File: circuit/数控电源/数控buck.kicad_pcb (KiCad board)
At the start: 2 copper layers, 60 x 60 mm, 79 parts, among them J1 Conn_01x06_MountingPin, J2 Conn_01x02, J3 Conn_01x02, J4 Conn_01x04_MountingPin, Q1 BSC070N10NS3G, Q2 BSC070N10NS3G, SW1 SW_Push, U1 STM32F334R8Tx, U2 LM5164DDA, U3 LM1117DT-3.3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

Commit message: finish circuir_V1.0
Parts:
- removed C18, C20, C21: 10p, Capacitor_SMD:C_0603_1608Metric
- removed C19: 1n, Capacitor_SMD:C_0603_1608Metric
- removed J3: Conn_01x02, Connector_AMASS:AMASS_XT30PW-M_1x02_P2.50mm_Horizontal
- added C36: 10u, Capacitor_SMD:C_1206_3216Metric, F.Cu at (131.5, 26.0)
- added C37: 22u, Capacitor_SMD:C_0805_2012Metric_Pad1.18x1.45mm_HandSolder, F.Cu at (125.5, 54.5)
- added C38: 10u, Capacitor_SMD:C_1206_3216Metric, F.Cu at (131.5, 29.2)
- added J5: Conn_01x02, Connector_AMASS:AMASS_XT30U-F_1x02_P5.0mm_Vertical, F.Cu at (162.2, 60.8)
- C1, C11, C2, C3, C4, C5, D1, L1, R1, R2, R3, R4, SW1, U2, U4: moved to F.Cu
- C12, C13: footprint Capacitor_SMD:CP_Elec_16x17.5 -> Capacitor_SMD:CP_Elec_10x10.5
- C17: value 10p -> 100n; moved to B.Cu
- C22, C23, R20: moved to B.Cu
- C31: footprint Capacitor_SMD:CP_Elec_6.3x7.7 -> Capacitor_Tantalum_SMD:CP_EIA-7343-31_Kemet-D
- C6: value C_Polarized -> 22u; footprint Capacitor_SMD:CP_Elec_6.3x4.5 -> Capacitor_SMD:C_0805_2012Metric_Pad1.18x1.45mm_HandSolder; moved to F.Cu
- J2: footprint Connector_AMASS:AMASS_XT30PW-F_1x02_P2.50mm_Horizontal -> Connector_AMASS:AMASS_XT30U-M_1x02_P5.0mm_Vertical; moved to F.Cu
- R12, R13: value 82 -> 1; moved to B.Cu
- R14: value 1.2k -> 1; moved to B.Cu
- R15: value 1.2k -> R; footprint Resistor_SMD:R_0603_1608Metric_Pad0.98x0.95mm_HandSolder -> Resistor_SMD:R_0805_2012Metric_Pad1.20x1.40mm_HandSolder
- R19: value 2 -> R; footprint Resistor_SMD:R_0603_1608Metric_Pad0.98x0.95mm_HandSolder -> Resistor_SMD:R_0805_2012Metric_Pad1.20x1.40mm_HandSolder; moved to B.Cu
- R9: footprint Resistor_SMD:R_0603_1608Metric_Pad0.98x0.95mm_HandSolder -> Resistor_SMD:R_0603_1608Metric; moved to F.Cu
- U5: value TLV9062 -> INA240A1PW; footprint Package_SO:SOIC-8_3.9x4.9mm_P1.27mm -> Package_SO:TSSOP-8_4.4x3mm_P0.65mm; moved to B.Cu
- moved U6 96.9 mm to (157.2, 67.5), turned to 180 degrees
- moved C15 91.7 mm to (162.0, 47.8), turned to -90 degrees
- moved C26 90.5 mm to (160.8, 51.0), turned to 180 degrees
- moved C27 88.6 mm to (159.5, 47.5), turned to -90 degrees
- moved U5 84.2 mm to (146.2, 53.0), turned to 180 degrees
- moved R11 82.5 mm to (159.5, 40.8)
- moved C12 82.0 mm to (152.5, 50.0)
- moved R16 80.1 mm to (163.2, 68.2), turned to 180 degrees
- moved R17 78.6 mm to (163.2, 66.5)
- moved R13 77.4 mm to (161.8, 44.2)
- moved C22 72.4 mm to (158.2, 46.2), turned to 180 degrees
- moved R12 71.5 mm to (155.8, 44.2)
- moved R18 71.3 mm to (157.2, 63.5), turned to 180 degrees
- moved R21 69.9 mm to (132.6, 53.4)
- moved R20 66.2 mm to (128.0, 65.0), turned to 180 degrees
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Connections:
- C17 pad 1: Net-(U5A--) -> GNDA
- C17 pad 2: +24V -> /adc_cir
- C22 pad 1: GNDA -> Net-(U5--)
- C22 pad 2: +3.3V -> Net-(U5-+)
- J4 pad 1: /SDA -> /U1_RX
- J4 pad 2: /SCL -> /U1_TX
- R12 pad 1: Net-(U5A-+) -> Net-(U5-+)
- R13 pad 1: Net-(U5A--) -> Net-(U5--)
- R14 pad 1: GNDA -> /adc_cir
- R14 pad 2: Net-(U5A-+) -> /comp_cirurt
- R15 pad 1: Net-(U5B-+) -> GND
- R15 pad 2: Net-(U5A--) -> GNDPWR
- R19 pad 1: /comp_cirurt -> GNDA
- R19 pad 2: /adc_cir -> GND
- R7 pad 1: GNDPWR -> GND
- R8 pad 1: GNDPWR -> GND
- U1 pad 10: /SDA -> unconnected-(U1-PC2-Pad10)
- U1 pad 11: /SCL -> unconnected-(U1-PC3-Pad11)
- U1 pad 58: unconnected-(U1-PB6-Pad58) -> /U1_TX
- U1 pad 59: unconnected-(U1-PB7-Pad59) -> /U1_RX
- U4 pad 4: GNDPWR -> GND
- U5 pad 1: Net-(U5B-+) -> GNDA
- U5 pad 2: Net-(U5A--) -> Net-(U5-+)
- U5 pad 3: Net-(U5A-+) -> Net-(U5--)
- U5 pad 5: Net-(U5B-+) -> +3.3V
- U5 pad 6: /comp_cirurt -> GNDA
- U5 pad 7: /comp_cirurt -> +3.3V
- U5 pad 8: +3.3V -> /comp_cirurt
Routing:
- net +3.3V: track 0.00 -> 135.7 mm, vias 0 -> 3
- net GNDA: track 0.00 -> 73.1 mm, vias 0 -> 21
- net +12V: track 0.00 -> 69.7 mm, vias 0 -> 1
- net /HRTIM_+: track 0.00 -> 56.8 mm, vias 0 -> 2
- net /HRTIM_-: track 0.00 -> 54.8 mm, vias 0 -> 2
- net +5V: track 0.00 -> 44.0 mm
- net Net-(Q2-D): track 0.00 -> 24.7 mm
- net /comp_volt: track 0.00 -> 21.0 mm, vias 0 -> 1
- net GND: track 0.00 -> 20.9 mm, vias 0 -> 26
- net Net-(U5--): track 0.00 -> 19.9 mm
- net Net-(C4-Pad1): track 0.00 -> 19.6 mm, vias 0 -> 2
- net Net-(U5-+): track 0.00 -> 18.6 mm
- net +24V: track 0.00 -> 18.3 mm, vias 0 -> 2
- net /SWDIO: track 0.00 -> 16.0 mm
- net /SWCLK: track 0.00 -> 14.8 mm
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- added copper zone on F.Cu, net +24V
- added copper zone on F.Cu, net +48V
- added copper zone on In2.Cu, net +48V
- added copper zone on B.Cu, net GND
- added copper zone on F.Cu, net GND
- added copper zone on In1.Cu, net GND
- added copper zone on B.Cu, net GNDA
- added copper zone on F.Cu, net GNDA
- added copper zone on F.Cu, net GNDPWR
- added copper zone on F.Cu, net Net-(L2-Pad2)
- added copper zone on F.Cu, net Net-(Q2-D)
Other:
- copper layers 2 -> 4

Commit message: 配置了dac和comp和hrtim定时器
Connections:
- C11 pad 2: Net-(C11-Pad2) -> /NRST
- R9 pad 1: Net-(C11-Pad2) -> /NRST
- R9 pad 2: /NRST -> +3.3V
- SW1 pad 2: Net-(C11-Pad2) -> /NRST
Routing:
- net GNDA: track 73.1 -> 86.3 mm, vias 21 -> 31
- net GND: track 20.9 -> 26.6 mm, vias 26 -> 77
- net +3.3V: track 135.7 -> 141.3 mm, vias 3 -> 4
- net Net-(C11-Pad2): track 4.89 -> 0.00 mm
- net +12V: track 69.7 -> 66.1 mm
- net /NRST: track 10.8 -> 14.0 mm
- net GNDPWR: track 0.00 -> 2.60 mm, vias 0 -> 6
- net +48V: vias 52 -> 40
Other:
- board text added: "呆呆"
- board text added: "数控buck_V1.0"

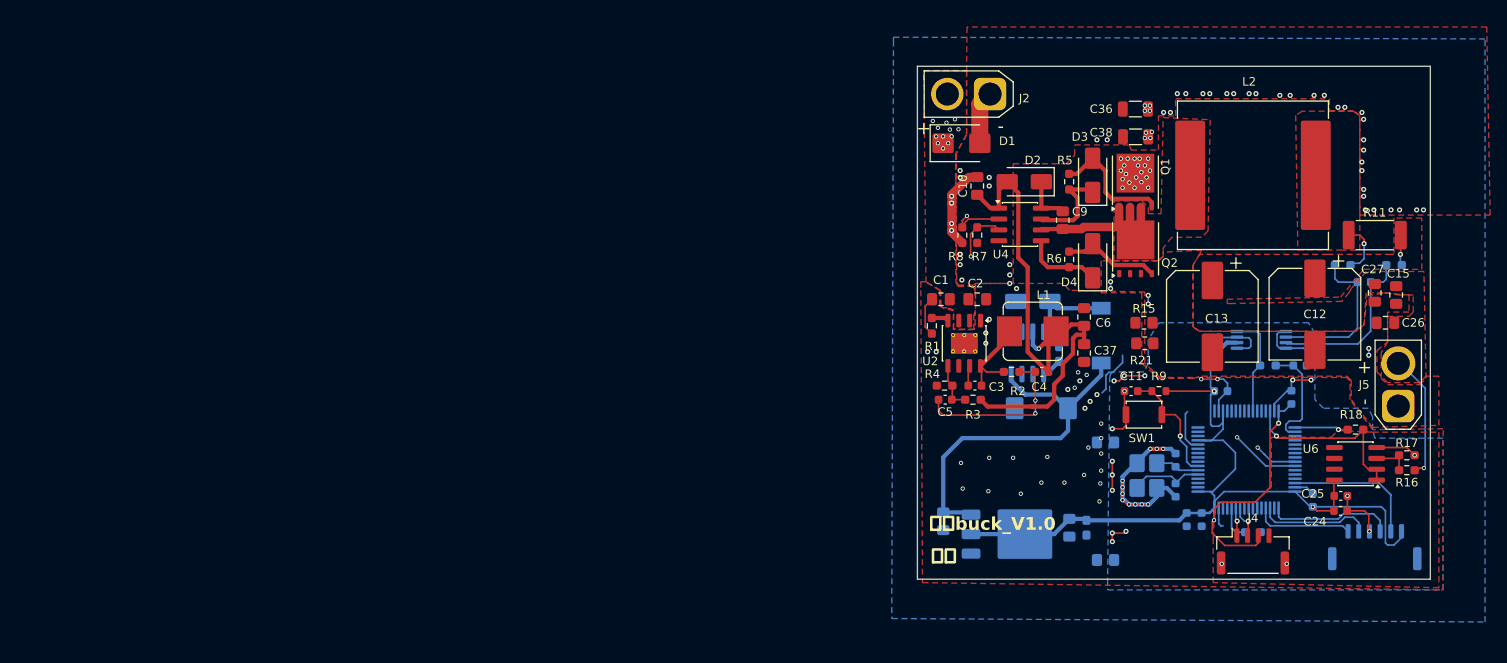
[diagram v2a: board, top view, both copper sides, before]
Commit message: recover second board layout
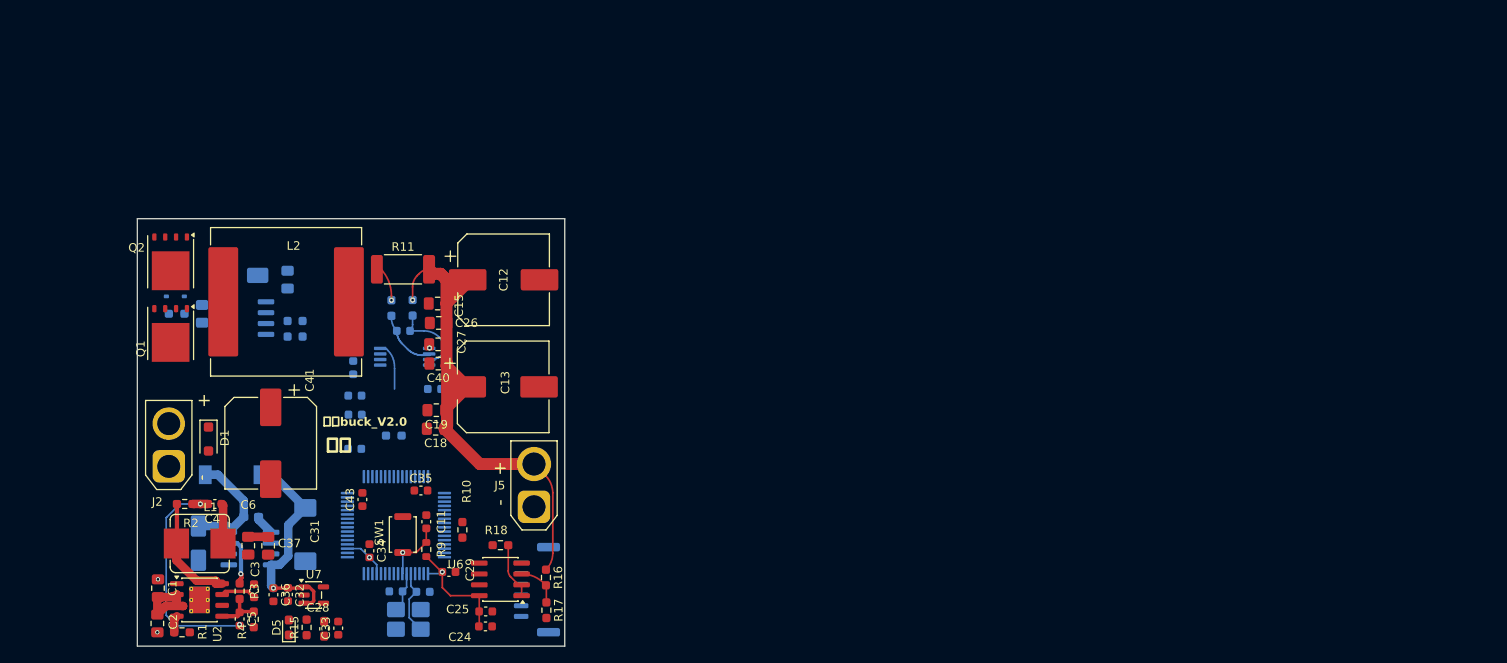
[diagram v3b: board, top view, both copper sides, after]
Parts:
- removed C38: 10u, Capacitor_SMD:C_1206_3216Metric
- removed C7, C8: 22u, Capacitor_SMD:C_0805_2012Metric_Pad1.18x1.45mm_HandSolder
- removed J4: Conn_01x04_MountingPin, Connector_JST:JST_GH_SM04B-GHS-TB_1x04-1MP_P1.25mm_Horizontal
- removed R19, R20, R21: R, Resistor_SMD:R_0805_2012Metric_Pad1.20x1.40mm_HandSolder
- removed U3: LM1117DT-3.3, Package_TO_SOT_SMD:TO-252-3_TabPin2
- added C18: 100u, Capacitor_SMD:C_0805_2012Metric_Pad1.18x1.45mm_HandSolder, F.Cu at (49.6, 63.4)
- added C19: 100u, Capacitor_SMD:C_0805_2012Metric_Pad1.18x1.45mm_HandSolder, F.Cu at (49.7, 61.2)
- added C20: 100n, Capacitor_SMD:C_0603_1608Metric, B.Cu at (40.2, 65.8)
- added C21: 100n, Capacitor_SMD:C_0603_1608Metric, B.Cu at (40.2, 59.5)
- added C39: 2.2u, Capacitor_SMD:C_0603_1608Metric, B.Cu at (40.2, 61.8)
- added C40: 100u, Capacitor_SMD:C_0805_2012Metric_Pad1.18x1.45mm_HandSolder, F.Cu at (50.0, 55.8)
- added C41: 100u, Capacitor_SMD:CP_Elec_10x10.5, F.Cu at (30.4, 65.1)
- added C43: 100n, Capacitor_SMD:C_0603_1608Metric, F.Cu at (41.1, 71.7)
- added D5: LED, LED_SMD:LED_0603_1608Metric_Pad1.05x0.95mm_HandSolder, F.Cu at (32.5, 86.7)
- added U7: ~, Package_TO_SOT_SMD:SOT-23-5, F.Cu at (35.4, 82.8)
- C10, C9, R5, R6, R7, R8, U4: moved to B.Cu
- C14, C16: value 10p -> 12p
- C26: value 100u -> 10u
- C28, R10: moved to F.Cu
- C29, C33, C34, C35: value 10p -> 100n; moved to F.Cu
- C32: value 10p -> 100nf; moved to F.Cu
- C36: value 10u -> 100nf; footprint Capacitor_SMD:C_1206_3216Metric -> Capacitor_SMD:C_0603_1608Metric
- D1: footprint Diode_SMD:D_SMB -> Diode_SMD:D_SOD-123F
- D2: value SS34 -> SS26; moved to B.Cu
- D3, D4: value SS34 -> B5819WS; footprint Diode_SMD:D_SMA -> Diode_SMD:D_SOD-323; moved to B.Cu
- L2: value 22u -> 33u
- R15: value R -> 11k; footprint Resistor_SMD:R_0805_2012Metric_Pad1.20x1.40mm_HandSolder -> Resistor_SMD:R_0603_1608Metric_Pad0.98x0.95mm_HandSolder
- R16: value 44k -> 27k
- R17: value 4k -> 3k
- moved C36 115.7 mm to (30.7, 82.8), turned to -90 degrees
- moved C33 115.0 mm to (38.2, 86.7), turned to 90 degrees
- moved R13 114.9 mm to (47.0, 49.2), turned to 90 degrees
- moved Q1 114.2 mm to (18.6, 52.2), turned to -90 degrees
- moved L2 114.1 mm to (32.1, 48.5)
- moved R11 113.7 mm to (45.8, 44.8)
- moved Q2 112.9 mm to (18.6, 43.9), turned to -90 degrees
- moved C22 112.5 mm to (45.9, 52.0)
- moved C15 112.1 mm to (49.9, 48.8), turned to 180 degrees
- moved R12 111.4 mm to (44.5, 49.3), turned to 90 degrees
- moved C26 110.8 mm to (50.0, 51.0)
- moved C27 109.7 mm to (49.9, 53.5), turned to 180 degrees
- moved D3 108.2 mm to (19.2, 47.9), turned to 180 degrees
- moved D4 107.7 mm to (19.3, 54.1), turned to 180 degrees
- moved R5 105.5 mm to (19.3, 49.9), turned to 180 degrees
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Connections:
- C11 pad 1: GNDA -> GND
- C12 pad 2: GNDPWR -> GND
- C13 pad 2: GNDPWR -> GND
- C14 pad 1: GNDA -> GND
- C15 pad 2: GNDPWR -> GND
- C16 pad 1: GNDA -> GND
- C17 pad 1: GNDA -> GND
- C23 pad 1: GNDA -> GND
- C24 pad 1: GNDA -> Net-(C24-Pad1)
- C25 pad 1: GNDA -> Net-(C24-Pad1)
- C26 pad 2: GNDPWR -> GND
- C27 pad 2: GNDPWR -> GND
- C29 pad 1: GNDA -> GND
- C32 pad 1: GNDA -> +5V
- C32 pad 2: +3.3V -> GND
- C33 pad 1: GNDA -> GND
- C34 pad 1: GNDA -> GND
- C35 pad 1: GNDA -> GND
- C36 pad 1: GND -> +5V
- C36 pad 2: +48V -> GND
- J1 pad 4: GNDA -> GND
- J1 pad MP: GNDA -> GND
- J5 pad 1: GNDPWR -> GND
- Q2 pad 1: GNDPWR -> GND
- Q2 pad 2: GNDPWR -> GND
- Q2 pad 3: GNDPWR -> GND
- R10 pad 1: GNDA -> GND
- R15 pad 1: GND -> Net-(D5-A)
- R15 pad 2: GNDPWR -> +3.3V
- R17 pad 2: GNDA -> GND
- SW1 pad 1: GNDA -> GND
- U1 pad 12: GNDA -> GND
- U1 pad 18: GNDA -> GND
- U1 pad 31: GNDA -> GND
- U1 pad 47: GNDA -> GND
- U1 pad 58: /U1_TX -> unconnected-(U1-PB6-Pad58)
- U1 pad 59: /U1_RX -> unconnected-(U1-PB7-Pad59)
- U1 pad 63: GNDA -> GND
- U5 pad 1: GNDA -> GND
- U5 pad 4: GNDA -> GND
- U5 pad 6: GNDA -> GND
- U6 pad 4: GNDA -> GND
- Y1 pad 2: GNDA -> GND
- Y1 pad 4: GNDA -> GND
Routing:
- net +3.3V: track 141.3 -> 19.8 mm, vias 4 -> 2
- net GNDA: track 86.3 -> 0.00 mm, vias 31 -> 0
- net /HRTIM_+: track 56.8 -> 0.00 mm, vias 2 -> 0
- net /HRTIM_-: track 54.8 -> 0.00 mm, vias 2 -> 0
- net +12V: track 66.1 -> 13.2 mm
- net +24V: track 18.3 -> 67.2 mm, vias 2 -> 1
- net GND: track 26.6 -> 0.06 mm, vias 77 -> 3
- net Net-(Q2-D): track 24.7 -> 0.00 mm
- net +5V: track 44.0 -> 26.0 mm, vias 0 -> 1
- net /SWDIO: track 16.0 -> 0.00 mm
- net /SWCLK: track 14.8 -> 0.00 mm
- net Net-(D3-A): track 14.6 -> 0.00 mm
- net /comp_volt: track 21.0 -> 7.32 mm, vias 1 -> 0
- net /USART3_TX: track 13.2 -> 0.00 mm
- net /adc_cir: track 12.7 -> 0.00 mm
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- removed copper zone on F.Cu, net +24V
- removed copper zone on F.Cu, net +48V
- removed copper zone on In2.Cu, net +48V
- removed copper zone on B.Cu, net GND
- removed copper zone on F.Cu, net GND
- removed copper zone on In1.Cu, net GND
- removed copper zone on B.Cu, net GNDA
- removed copper zone on F.Cu, net GNDA
- removed copper zone on F.Cu, net GNDPWR
- removed copper zone on F.Cu, net Net-(L2-Pad2)
- removed copper zone on F.Cu, net Net-(Q2-D)
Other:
- board size 60 x 60 mm -> 50 x 50 mm
- copper layers 4 -> 2
- board text added: "数控buck_V2.0"
- board text removed: "数控buck_V1.0"

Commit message: 完成第二版电路版布局
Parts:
- removed C17, C20: 100n, Capacitor_SMD:C_0603_1608Metric
- removed C23, C39: 2.2u, Capacitor_SMD:C_0603_1608Metric
- removed C41: 100u, Capacitor_SMD:CP_Elec_10x10.5
- added C38: 10u, Capacitor_SMD:C_1210_3225Metric, F.Cu at (23.4, 43.2)
- added C7: 10u, Capacitor_SMD:C_1210_3225Metric, F.Cu at (20.0, 43.3)
- added C8: 10u, Capacitor_SMD:C_1210_3225Metric_Pad1.33x2.70mm_HandSolder, F.Cu at (23.3, 49.1)
- added R19: 27k, Resistor_SMD:R_0603_1608Metric_Pad0.98x0.95mm_HandSolder, B.Cu at (23.3, 50.3)
- added R20: 3k, Resistor_SMD:R_0603_1608Metric_Pad0.98x0.95mm_HandSolder, B.Cu at (23.4, 54.3)
- added U3: TLV9062, Package_SO:SOIC-8_3.9x4.9mm_P1.27mm, B.Cu at (27.6, 59.1)
- C24, C25, R16, R17, R18, U6: moved to B.Cu
- J1: moved to F.Cu
- R11: footprint Resistor_SMD:R_2512_6332Metric_Pad1.40x3.35mm_HandSolder -> Resistor_SMD:R_1206_3216Metric_Pad1.30x1.75mm_HandSolder
- moved C2 26.3 mm to (17.0, 59.9), turned to 180 degrees
- moved R1 24.8 mm to (16.0, 62.8), turned to -90 degrees
- moved C1 22.5 mm to (21.1, 59.9), turned to 0 degrees
- moved C24 22.3 mm to (55.0, 64.2), turned to 0 degrees
- moved C25 22.2 mm to (55.0, 62.5), turned to 0 degrees
- moved D1 22.2 mm to (16.8, 43.3), turned to 90 degrees
- moved U2 18.8 mm to (19.8, 64.8), turned to -90 degrees
- moved C5 18.6 mm to (17.6, 69.5), turned to 180 degrees
- moved R4 18.2 mm to (17.5, 71.2), turned to 0 degrees
- moved R16 14.3 mm to (63.2, 66.5)
- moved R17 14.3 mm to (63.2, 70.4)
- moved R3 14.2 mm to (20.8, 69.5), turned to 0 degrees
- moved R2 14.0 mm to (31.1, 63.2), turned to -90 degrees
- moved C3 13.5 mm to (20.9, 71.2), turned to 0 degrees
- moved J2 13.4 mm to (18.3, 54.4)
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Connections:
- U1 pad 35: unconnected-(U1-PB14-Pad35) -> /adc_Vin
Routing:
- net +24V: track 67.2 -> 0.00 mm, vias 1 -> 0
- net Net-(C4-Pad1): track 27.1 -> 0.00 mm, vias 2 -> 0
- net +5V: track 26.0 -> 0.00 mm, vias 1 -> 0
- net +3.3V: track 19.8 -> 0.00 mm, vias 2 -> 0
- net Net-(D13-K): track 13.6 -> 0.00 mm
- net Net-(U2-SW): track 13.3 -> 0.00 mm
- net +12V: track 13.2 -> 0.00 mm, vias 1 -> 0
- net Net-(U5--): track 9.00 -> 0.00 mm
- net /OSC_IN: track 7.68 -> 0.00 mm
- net Net-(U5-+): track 7.56 -> 0.00 mm
- net /NRST: track 7.38 -> 0.00 mm, vias 1 -> 0
- net /comp_volt: track 7.32 -> 0.00 mm
- net Net-(U2-FB): track 5.77 -> 0.00 mm
- net /comp_cirurt: track 5.53 -> 0.00 mm
- net Net-(U6A-+): track 5.24 -> 0.00 mm
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- added copper zone on F.Cu, net +24V
- added copper zone on F.Cu, net +48V
- added copper zone on F.Cu, net Net-(L2-Pad2)
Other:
- board size 50 x 50 mm -> 56.4 x 40.5 mm
- board text added: "数控buck_V2"
- board text removed: "数控buck_V2.0"
